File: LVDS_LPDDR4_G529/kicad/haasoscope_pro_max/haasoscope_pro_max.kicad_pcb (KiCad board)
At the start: 10 copper layers, 200 x 125 mm, 8 parts, among them IC1 ADC12DL500ACF_Aligned, U1 MT53D512M16D1DS_Aligned, U2 FT601Q_Aligned, U3 Ti90G529_Functions

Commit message: grid router fixes
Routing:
- net Net-(U2A-DATA_2): track 0.00 -> 23.6 mm, vias 0 -> 3
- net Net-(U2A-DATA_5): track 0.00 -> 22.1 mm, vias 1 -> 3
- net Net-(U2A-DATA_11): track 0.00 -> 22.0 mm, vias 1 -> 2
- net Net-(U2A-DATA_3): track 0.00 -> 21.8 mm, vias 1 -> 3
- net Net-(U2A-DATA_1): track 0.00 -> 21.5 mm, vias 1 -> 3
- net Net-(U2A-DATA_14): track 0.00 -> 20.8 mm, vias 1 -> 2
- net Net-(U2A-DATA_7): track 0.00 -> 20.7 mm, vias 1 -> 3
- net Net-(U2A-DATA_4): track 0.00 -> 20.6 mm, vias 1 -> 2
- net Net-(U2A-DATA_8): track 0.00 -> 19.8 mm, vias 1 -> 2
- net Net-(U2A-DATA_6): track 0.00 -> 19.2 mm, vias 1 -> 3
- net Net-(U2A-DATA_9): track 0.00 -> 18.9 mm, vias 1 -> 2
- net Net-(U2A-DATA_17): track 0.00 -> 18.4 mm, vias 1 -> 2
- net Net-(U2A-DATA_20): track 0.00 -> 18.3 mm, vias 1 -> 2
- net Net-(U2A-DATA_10): track 0.00 -> 18.1 mm, vias 1 -> 3
- net Net-(U2A-DATA_13): track 0.00 -> 18.0 mm, vias 1 -> 3
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
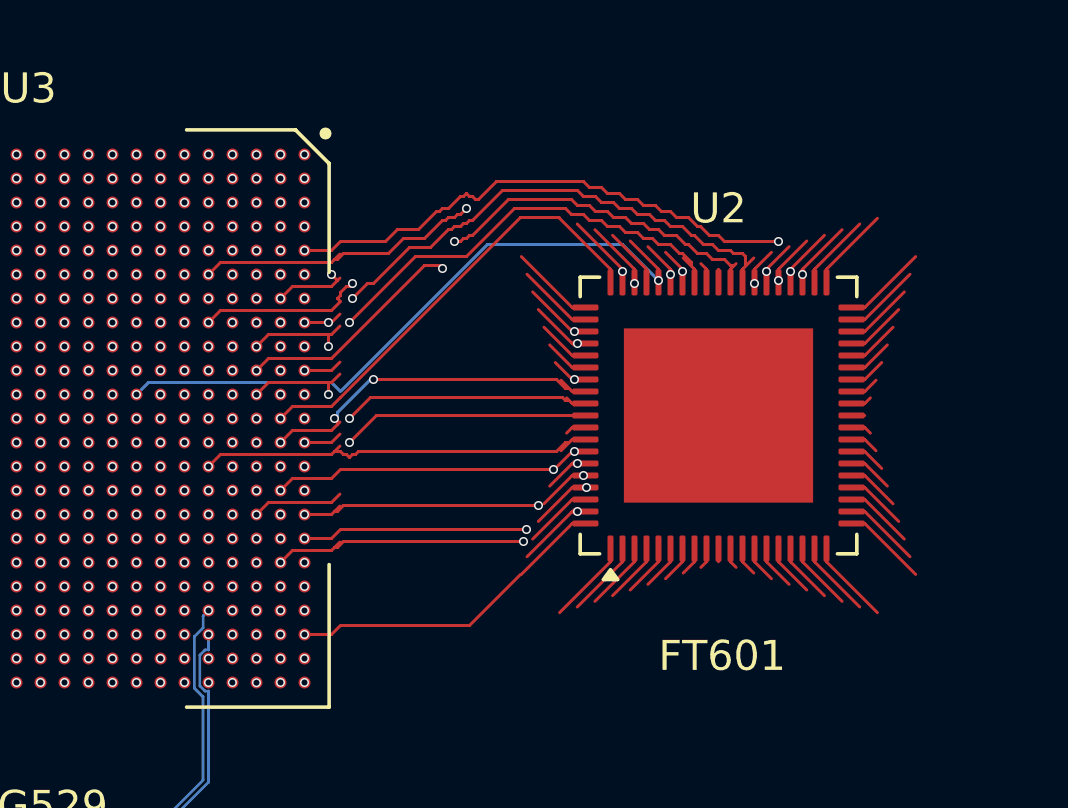
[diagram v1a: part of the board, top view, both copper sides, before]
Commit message: better via-track avoidance in bga zone
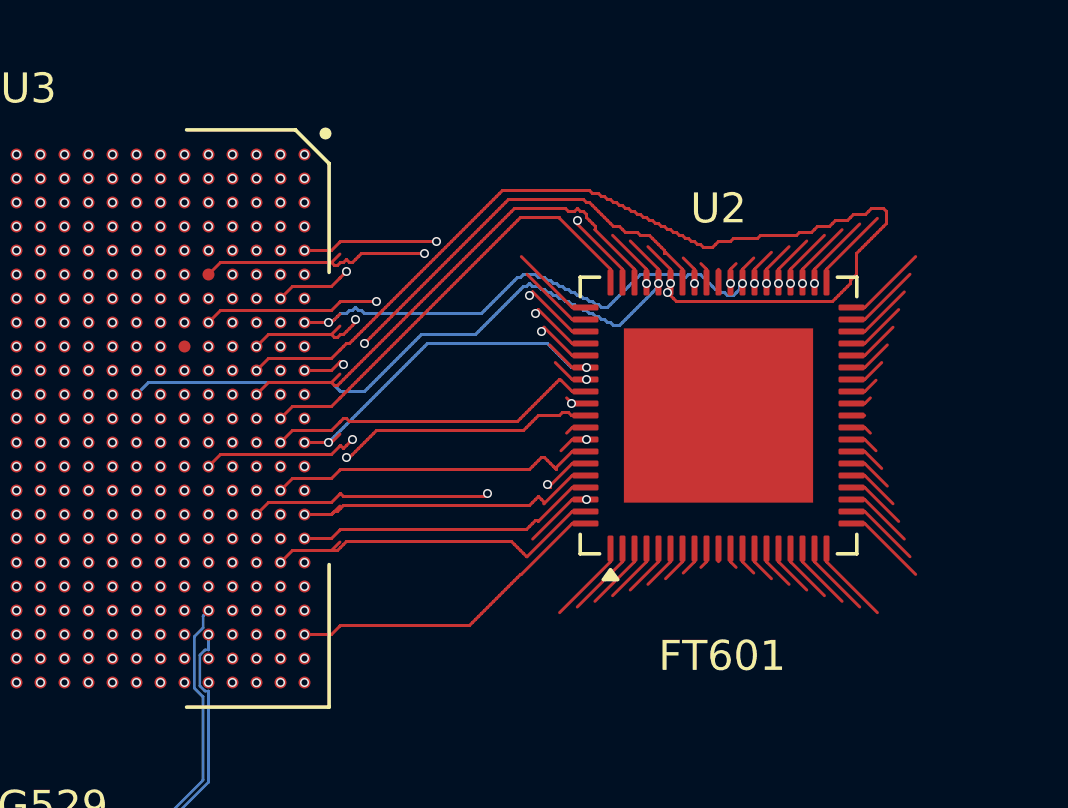
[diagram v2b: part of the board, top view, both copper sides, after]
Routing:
- net Net-(U2A-DATA_0): track 7.93 -> 29.2 mm
- net Net-(U2A-DATA_10): track 18.1 -> 36.2 mm
- net Net-(U2A-DATA_12): track 3.34 -> 17.1 mm, vias 1 -> 3
- net Net-(U2A-DATA_19): track 2.80 -> 13.2 mm, vias 1 -> 3
- net Net-(U2A-DATA_29): track 5.37 -> 14.0 mm, vias 1 -> 3
- net Net-(U2A-DATA_18): track 5.53 -> 13.4 mm, vias 1 -> 2
- net Net-(U2A-DATA_17): track 18.4 -> 16.2 mm
- net Net-(U2A-DATA_28): track 12.1 -> 10.1 mm, vias 3 -> 1
- net Net-(U2A-DATA_30): track 13.5 -> 11.7 mm, vias 3 -> 1
- net Net-(U2A-DATA_1): track 21.5 -> 19.8 mm
- net Net-(U2A-DATA_16): track 16.4 -> 14.7 mm
- net Net-(U2A-DATA_14): track 20.8 -> 19.1 mm
- net Net-(U2A-DATA_24): track 13.7 -> 15.2 mm, vias 1 -> 3
- net Net-(U2A-DATA_27): track 11.9 -> 10.5 mm, vias 3 -> 1
- net Net-(U2A-DATA_26): track 12.8 -> 11.7 mm
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
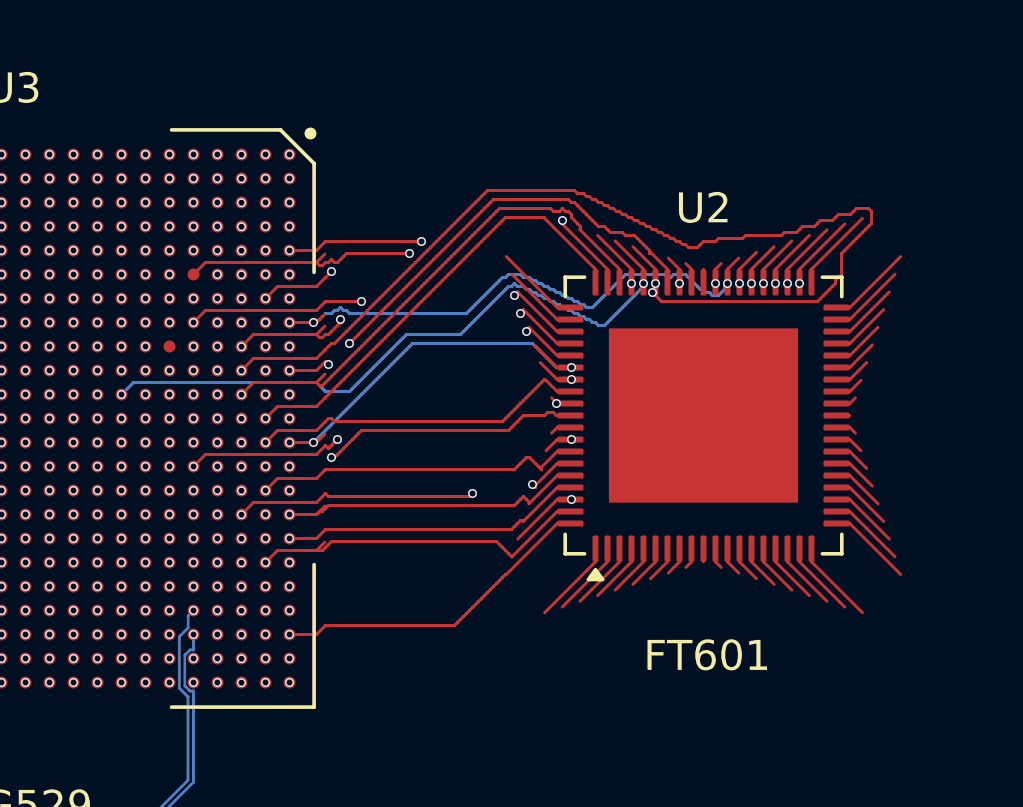
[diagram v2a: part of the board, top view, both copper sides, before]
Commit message: inside out ordering of bga nets
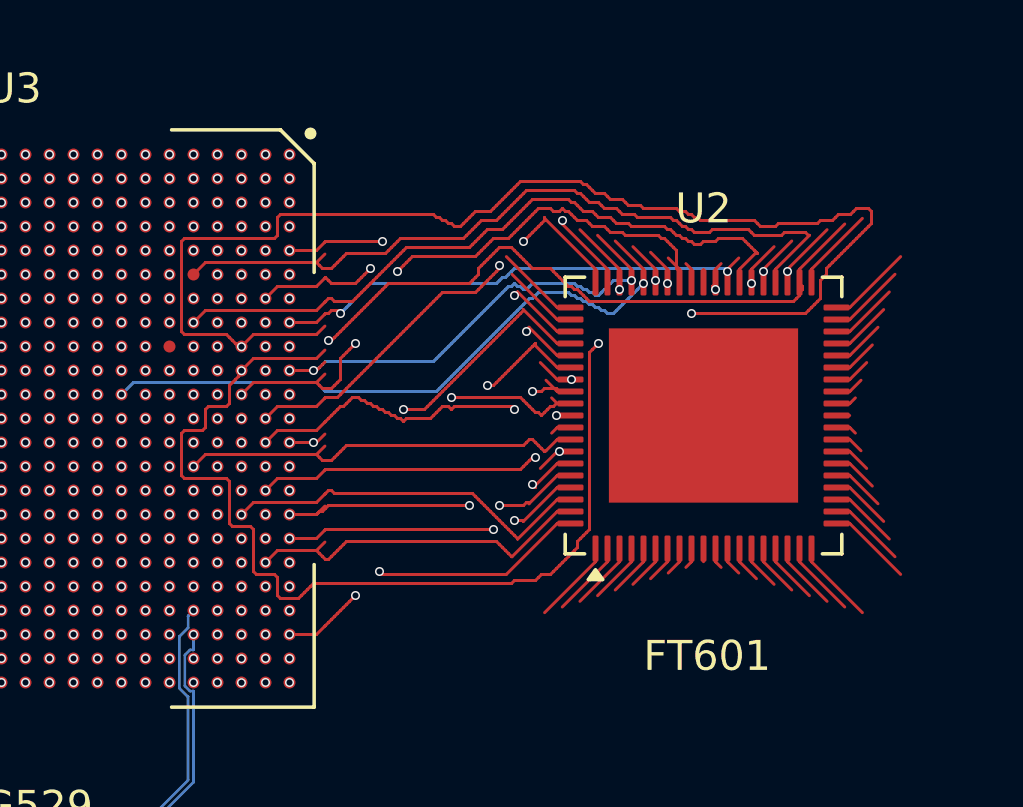
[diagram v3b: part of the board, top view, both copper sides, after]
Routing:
- net Net-(U2A-DATA_7): track 19.8 -> 44.0 mm
- net Net-(U2A-DATA_20): track 17.7 -> 21.7 mm
- net Net-(U2A-DATA_4): track 20.2 -> 23.5 mm
- net Net-(U2A-DATA_6): track 19.6 -> 16.9 mm
- net Net-(U2A-DATA_0): track 29.2 -> 26.5 mm
- net Net-(U2A-DATA_2): track 22.8 -> 25.1 mm, vias 2 -> 0
- net Net-(U2A-DATA_21): track 11.3 -> 12.8 mm, vias 1 -> 3
- net Net-(U2A-DATA_13): track 17.2 -> 18.6 mm, vias 1 -> 3
- net Net-(U2A-DATA_29): track 14.0 -> 12.5 mm, vias 3 -> 1
- net Net-(U2A-DATA_24): track 15.2 -> 13.8 mm, vias 3 -> 1
- net Net-(U2A-DATA_10): track 36.2 -> 37.3 mm
- net Net-(U2A-DATA_8): track 19.9 -> 20.9 mm
- net Net-(U2A-DATA_3): track 21.5 -> 22.4 mm
- net Net-(U2A-DATA_25): track 11.1 -> 12.0 mm, vias 1 -> 3
- net Net-(U2A-DATA_19): track 13.2 -> 12.4 mm
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
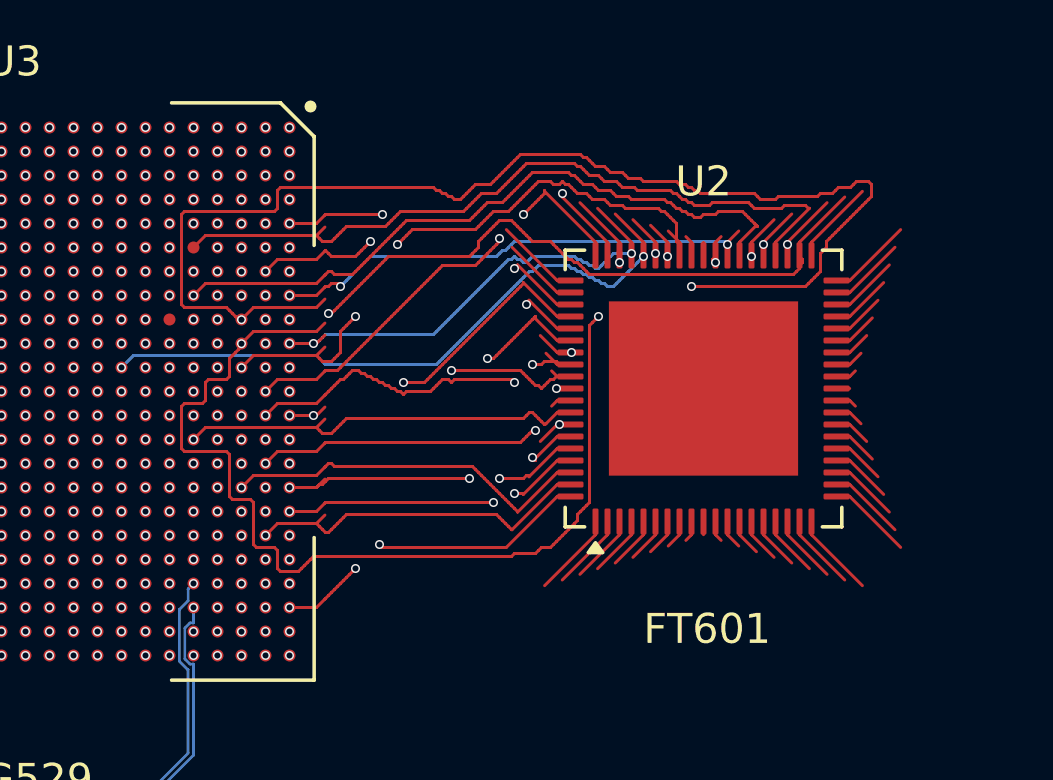
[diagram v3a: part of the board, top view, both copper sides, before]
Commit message: Block routing on top layer through bga
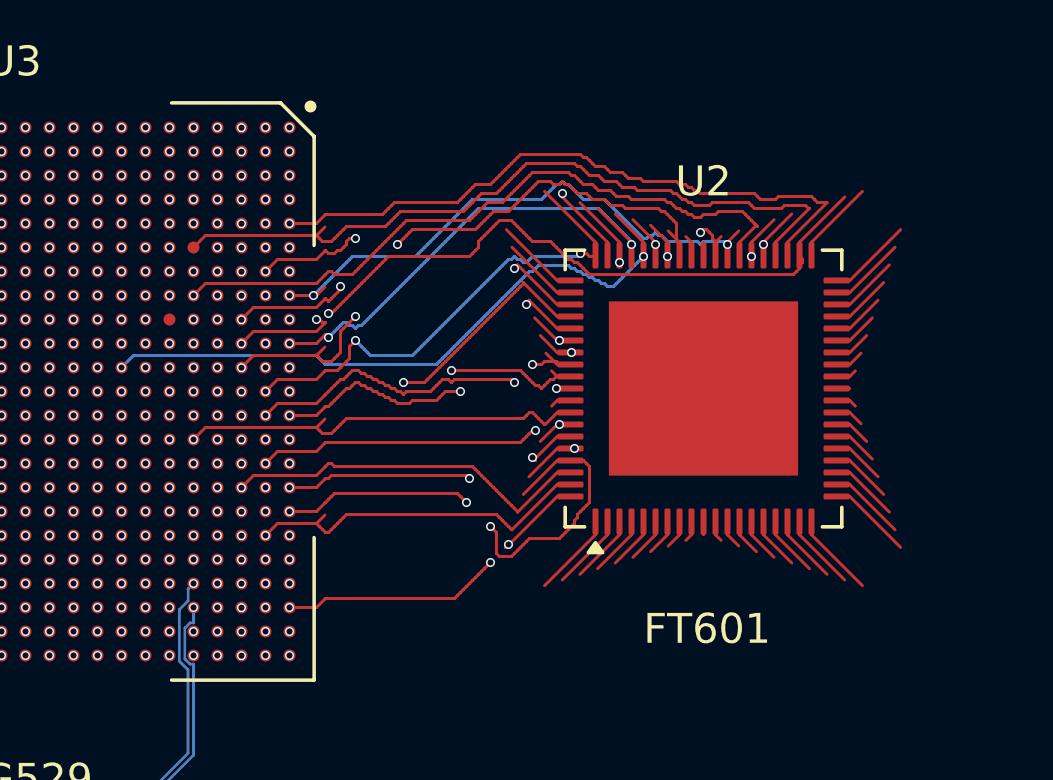
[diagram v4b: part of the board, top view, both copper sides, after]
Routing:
- net Net-(U2A-DATA_7): track 44.0 -> 19.5 mm
- net Net-(U2A-DATA_10): track 37.3 -> 19.8 mm
- net Net-(U2A-DATA_28): track 10.1 -> 16.3 mm
- net Net-(U2A-DATA_6): track 16.9 -> 19.3 mm
- net Net-(U2A-DATA_27): track 10.4 -> 12.3 mm
- net Net-(U2A-DATA_15): track 15.1 -> 16.6 mm
- net Net-(U2A-DATA_1): track 20.6 -> 21.9 mm, vias 3 -> 1
- net Net-(U2A-DATA_4): track 23.5 -> 22.8 mm
